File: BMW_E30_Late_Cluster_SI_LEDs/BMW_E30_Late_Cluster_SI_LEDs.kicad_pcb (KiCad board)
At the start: 2 copper layers, 57.8 x 34.5 mm, 11 parts, among them J1 SI Board Connector

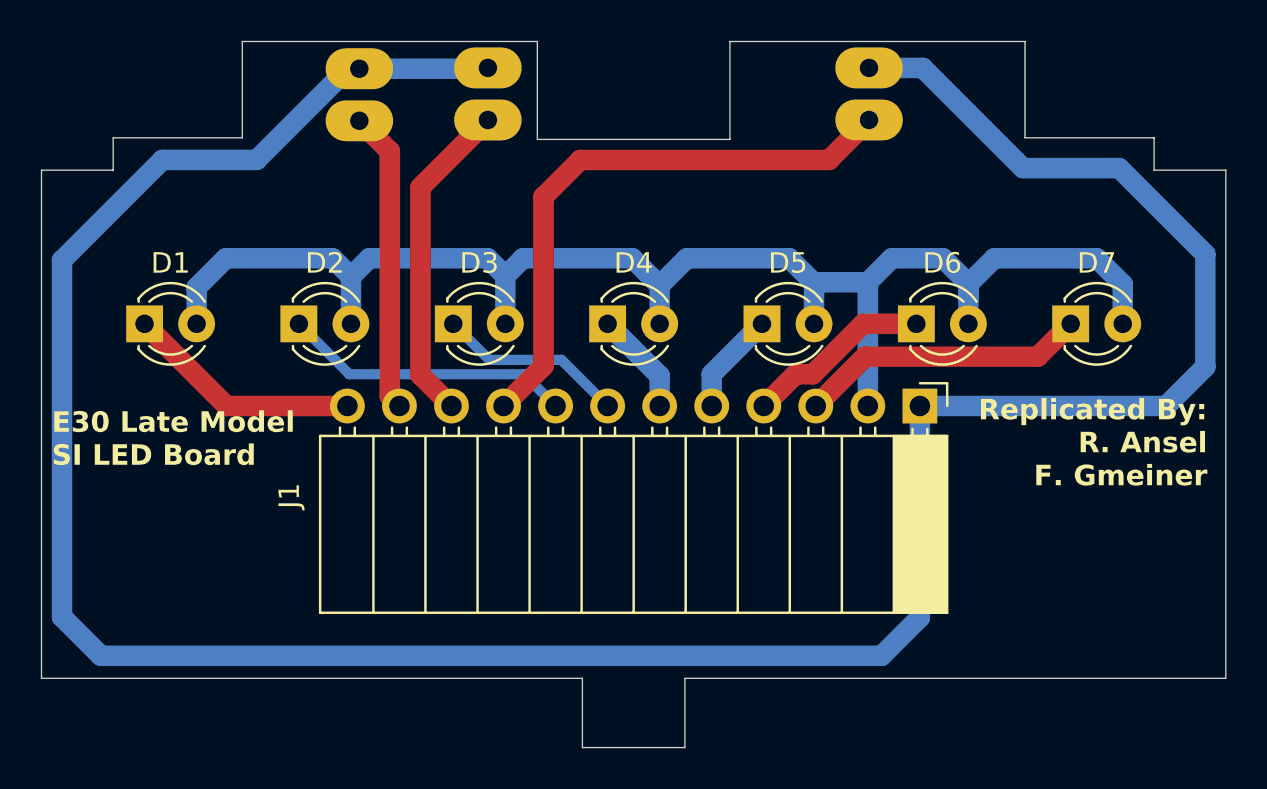
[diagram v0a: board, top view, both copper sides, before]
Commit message: Board Styling on SI and SI LED
Added fillets to the SI and SI_LED boards and generated the first gbr files for pricing estimation on JLC.
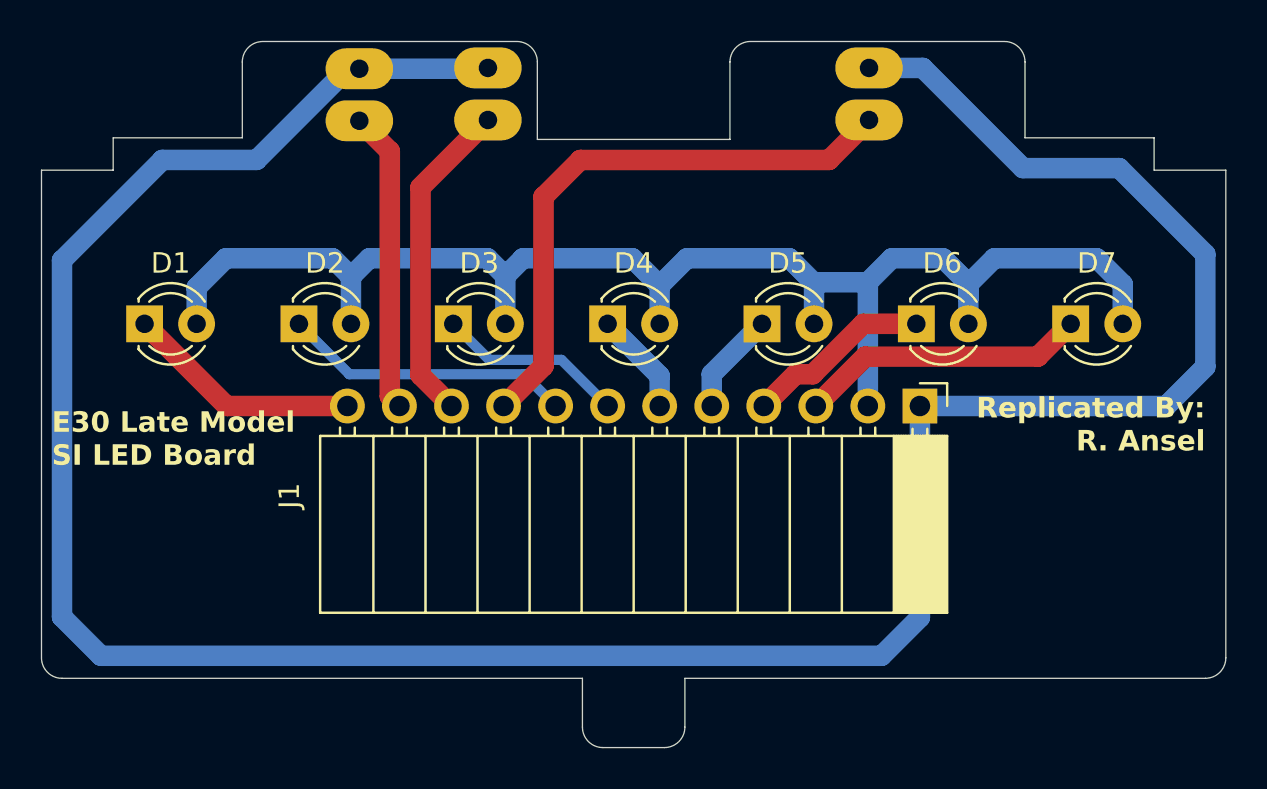
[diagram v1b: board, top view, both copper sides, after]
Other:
- outline, holes or cut-outs redrawn
- board text added: "Replicated By: R. Ansel"
- board text removed: "Replicated By: R. Ansel F. Gmeiner"
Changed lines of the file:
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@@
 			(outputformat 1)
 			(mirror no)
-			(drillshape 1)
+			(drillshape 0)
 			(scaleselection 1)
-			(outputdirectory "")
+			(outputdirectory "/home/nomics/main/Documents/[01] Projects/KiCad Projects/SI_LED_GBR/")
 		)
 	)
@@
 		)
 	)
+	(gr_arc
+		(start 101 100)
+		(mid 100.292893 99.707107)
+		(end 100 99)
+		(stroke
+			(width 0.05)
+			(type default)
+		)
+		(layer "Edge.Cuts")
+	)
 	(gr_line
-		(start 157.8 100)
+		(start 157.8 99)
 		(end 157.8 75.2)
 		(stroke
@@
 	)
 	(gr_line
-		(start 133.6 68.92)
+		(start 133.6 69.92)
 		(end 133.6 73.7)
 		(stroke
@@
 	(gr_line
 		(start 109.8 73.62)
-		(end 109.8 68.92)
+		(end 109.8 69.92)
 		(stroke
 			(width 0.05)
@@
 	)
 	(gr_line
-		(start 109.8 68.92)
-		(end 124.2 68.92)
+		(start 110.8 68.92)
+		(end 123.2 68.92)
 		(stroke
 			(width 0.05)
@@
 		(layer "Edge.Cuts")
 	)
+	(gr_arc
+		(start 127.4 103.38)
+		(mid 126.692893 103.087107)
+		(end 126.4 102.38)
+		(stroke
+			(width 0.05)
+			(type default)
+		)
+		(layer "Edge.Cuts")
+	)
+	(gr_arc
+		(start 157.8 99)
+		(mid 157.507107 99.707107)
+		(end 156.8 100)
+		(stroke
+			(width 0.05)
+			(type default)
+		)
+		(layer "Edge.Cuts")
+	)
 	(gr_line
-		(start 124.2 68.92)
+		(start 124.2 69.92)
 		(end 124.2 73.7)
 		(stroke
@@
 		(layer "Edge.Cuts")
 	)
+	(gr_arc
+		(start 123.2 68.92)
+		(mid 123.907107 69.212893)
+		(end 124.2 69.92)
+		(stroke
+			(width 0.05)
+			(type default)
+		)
+		(layer "Edge.Cuts")
+	)
 	(gr_line
-		(start 157.8 100)
+		(start 156.8 100)
 		(end 131.4 100)
 		(stroke
@@
 	(gr_line
 		(start 126.4 100)
-		(end 126.4 103.38)
+		(end 126.4 102.38)
 		(stroke
 			(width 0.05)
@@
 		(layer "Edge.Cuts")
 	)
+	(gr_arc
+		(start 109.8 69.92)
+		(mid 110.092893 69.212893)
+		(end 110.8 68.92)
+		(stroke
+			(width 0.05)
+			(type default)
+		)
+		(layer "Edge.Cuts")
+	)
+	(gr_arc
+		(start 133.6 69.92)
+		(mid 133.892893 69.212893)
+		(end 134.6 68.92)
+		(stroke
+			(width 0.05)
+			(type default)
+		)
+		(layer "Edge.Cuts")
+	)
 	(gr_line
-		(start 100 100)
+		(start 100 99)
 		(end 100 75.2)
 		(stroke
@@
 		(layer "Edge.Cuts")
 	)
+	(gr_arc
+		(start 147 68.92)
+		(mid 147.707107 69.212893)
+		(end 148 69.92)
+		(stroke
+			(width 0.05)
+			(type default)
+		)
+		(layer "Edge.Cuts")
+	)
 	(gr_line
 		(start 154.3 73.62)
@@
 	)
 	(gr_line
-		(start 100 100)
+		(start 101 100)
 		(end 126.4 100)
 		(stroke
@@
 	(gr_line
 		(start 131.4 100)
-		(end 131.4 103.38)
+		(end 131.4 102.38)
 		(stroke
 			(width 0.05)
@@
 	)
 	(gr_line
-		(start 148 68.92)
-		(end 133.6 68.92)
+		(start 147 68.92)
+		(end 134.6 68.92)
 		(stroke
 			(width 0.05)
@@
 	)
 	(gr_line
-		(start 157.8 75.2)
-		(end 154.3 75.2)
+		(start 154.3 75.2)
+		(end 157.8 75.2)
 		(stroke
 			(width 0.05)
@@
 		(layer "Edge.Cuts")
 	)
+	(gr_arc
+		(start 131.4 102.38)
+		(mid 131.107107 103.087107)
+		(end 130.4 103.38)
+		(stroke
+			(width 0.05)
+			(type default)
+		)
+		(layer "Edge.Cuts")
+	)
 	(gr_line
 		(start 148 73.62)
-		(end 148 68.92)
+		(end 148 69.92)
 		(stroke
 			(width 0.05)
@@
 	)
 	(gr_line
-		(start 126.4 103.38)
-		(end 131.4 103.38)
+		(start 127.4 103.38)
+		(end 130.4 103.38)
 		(stroke
 			(width 0.05)
@@
 		(layer "User.1")
 	)
-	(gr_text "Replicated By:\nR. Ansel\nF. Gmeiner"
-		(at 156.9 90.7 0)
+	(gr_text "Replicated By:\nR. Ansel"
+		(at 156.8 89 0)
 		(layer "F.SilkS" knockout)
 		(effects
